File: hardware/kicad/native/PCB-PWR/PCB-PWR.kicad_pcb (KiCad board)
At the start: 4 copper layers, 90 x 60 mm, 66 parts, among them J1 43045-0213, J2 43045-1202, Q1 CSD18540Q5B, U1 LM74700QDBVRQ1, U2 INA226AIDGSR, U3 LMR604403SRAKR, U4 LMR604403SRAKR, U5 TPS7A2018PDBVR

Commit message: pcb-pwr: apply accepted C13-to-C11 routing 009
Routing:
- net VBAT_SYS: track 38.9 -> 70.3 mm
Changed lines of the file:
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@@
+		(net 31)
+	)
+	(segment
+		(start 44 31.8)
+		(end 44 27)
+		(width 3)
+		(layer "F.Cu")
+		(net 31)
+	)
+	(segment
+		(start 44 27)
+		(end 39 27)
+		(width 3)
+		(layer "F.Cu")
+		(net 31)
+	)
+	(segment
+		(start 39 27)
+		(end 39 14)
+		(width 3)
+		(layer "F.Cu")
+		(net 31)
+	)
+	(segment
+		(start 39 14)
+		(end 47.525 14)
+		(width 3)
+		(layer "F.Cu")
 		(net 31)
 	)

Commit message: pcb-pwr: apply accepted 3V8 output bulk routing 010
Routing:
- net 3V8_MODEM: track 0.00 -> 29.0 mm
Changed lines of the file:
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@@
 		(net 31)
+	)
+	(segment
+		(start 64.76 12)
+		(end 67.525 10)
+		(width 3)
+		(layer "F.Cu")
+		(net 3)
+	)
+	(segment
+		(start 64.76 17)
+		(end 67.525 17)
+		(width 3)
+		(layer "F.Cu")
+		(net 3)
+	)
+	(segment
+		(start 67.525 10)
+		(end 67.525 6.8)
+		(width 3)
+		(layer "F.Cu")
+		(net 3)
+	)
+	(segment
+		(start 67.525 6.8)
+		(end 72.525 6.8)
+		(width 3)
+		(layer "F.Cu")
+		(net 3)
+	)
+	(segment
+		(start 72.525 6.8)
+		(end 72.525 7.4)
+		(width 3)
+		(layer "F.Cu")
+		(net 3)
+	)
+	(segment
+		(start 72.525 7.4)
+		(end 72.525 10)
+		(width 0.5)
+		(layer "F.Cu")
+		(net 3)
+	)
+	(segment
+		(start 67.525 17)
+		(end 67.525 20.2)
+		(width 3)
+		(layer "F.Cu")
+		(net 3)
+	)
+	(segment
+		(start 67.525 20.2)
+		(end 72.525 20.2)
+		(width 3)
+		(layer "F.Cu")
+		(net 3)
+	)
+	(segment
+		(start 72.525 20.2)
+		(end 72.525 19.6)
+		(width 3)
+		(layer "F.Cu")
+		(net 3)
+	)
+	(segment
+		(start 72.525 19.6)
+		(end 72.525 17)
+		(width 0.5)
+		(layer "F.Cu")
+		(net 3)
 	)
 	(embedded_fonts no)

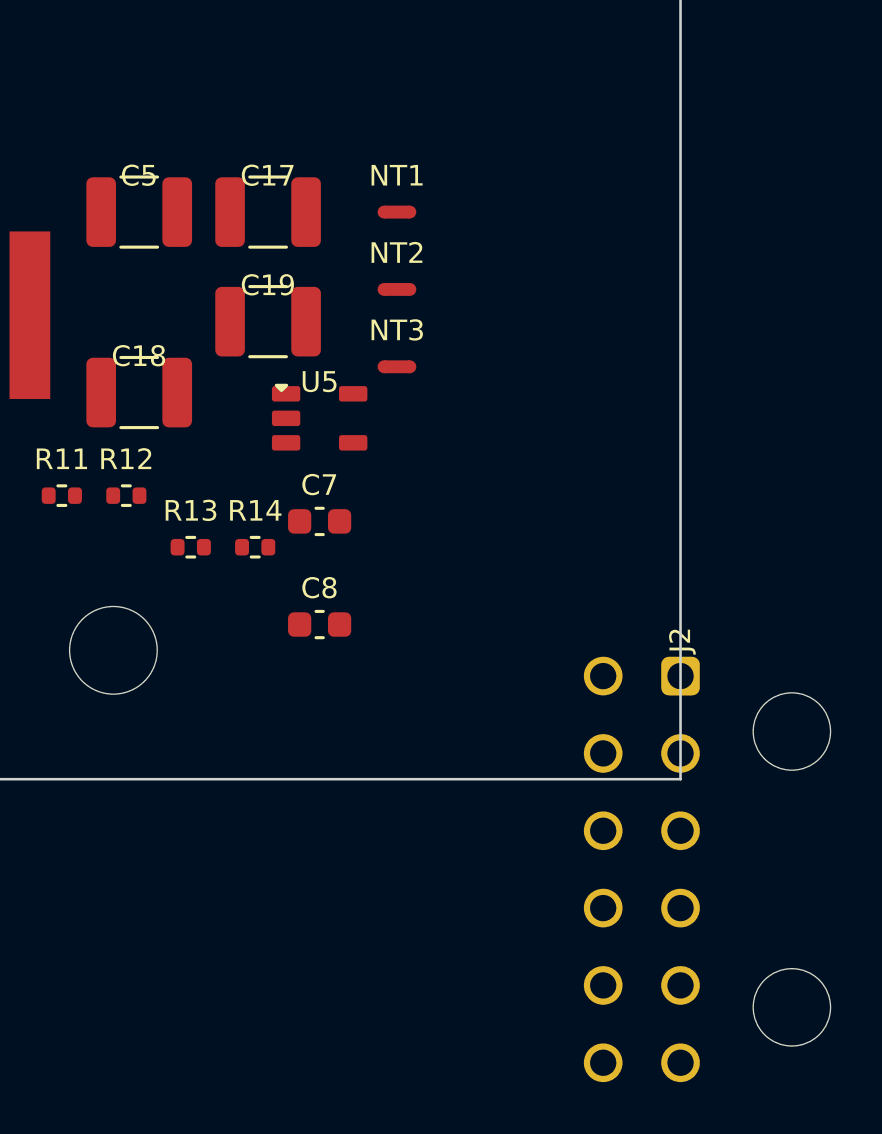
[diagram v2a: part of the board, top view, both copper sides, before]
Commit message: apply: tools/apply_pcb_pwr_j2_placement_eco_003_rev_a.py
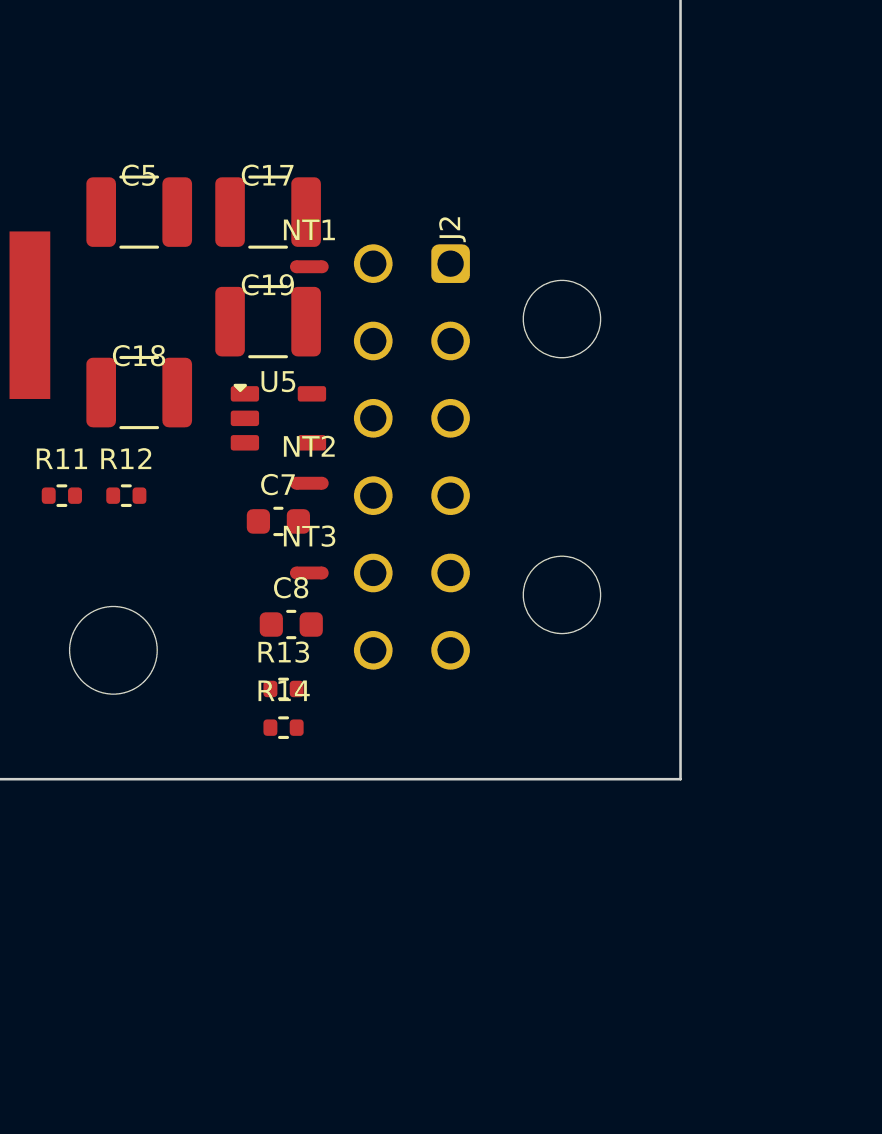
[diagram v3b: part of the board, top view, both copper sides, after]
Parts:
- moved J2 18.3 mm to (81.1, 40.0)
- moved NT3 8.69 mm to (75.6, 52.0)
- moved NT2 8.25 mm to (75.6, 48.5)
- moved R14 7.09 mm to (74.6, 58.0)
- moved R13 6.57 mm to (74.6, 56.5)
- moved NT1 4.01 mm to (75.6, 40.1)
- moved C7 1.60 mm to (74.4, 50.0)
- moved U5 1.60 mm to (74.4, 46.0)
- moved C8 1.10 mm to (74.9, 54.0)
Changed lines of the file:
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@@
 	(footprint "Capacitor_SMD:C_0603_1608Metric"
 		(layer "F.Cu")
-		(at 76 50)
+		(at 74.4 50)
 		(descr "DIONEA_PCB_PWR_REV_A|population=FITTED|zone=AUX_1V8|placement=PROVISIONAL_NOISE_REVIEW_PENDING|authority=PCB_PWR_PASSIVE_AUTHORITY_REV_A.csv")
 		(tags "DIONEA PCB-PWR EVT DIM-003 ACCEPTED NOT FOR MANUFACTURE")
@@
 	(footprint "NetTie:NetTie-2_SMD_Pad0.5mm"
 		(layer "F.Cu")
-		(at 79 38)
+		(at 75.6 40.12)
 		(descr "DIONEA_PCB_PWR_REV_A|population=PCB_FEATURE|zone=GROUND_JOIN|placement=PROVISIONAL_RETURN_REVIEW_PENDING|authority=PCB_PWR_PASSIVE_AUTHORITY_REV_A.csv")
 		(tags "DIONEA PCB-PWR EVT DIM-003 ACCEPTED NOT FOR MANUFACTURE")
@@
 	(footprint "NetTie:NetTie-2_SMD_Pad0.5mm"
 		(layer "F.Cu")
-		(at 79 41)
+		(at 75.6 48.52)
 		(descr "DIONEA_PCB_PWR_REV_A|population=PCB_FEATURE|zone=GROUND_JOIN|placement=PROVISIONAL_RETURN_REVIEW_PENDING|authority=PCB_PWR_PASSIVE_AUTHORITY_REV_A.csv")
 		(tags "DIONEA PCB-PWR EVT DIM-003 ACCEPTED NOT FOR MANUFACTURE")
@@
 	(footprint "Resistor_SMD:R_0402_1005Metric"
 		(layer "F.Cu")
-		(at 71 51)
+		(at 74.6 56.5)
 		(descr "DIONEA_PCB_PWR_REV_A|population=DNP|zone=CONTROL_INTERFACE|placement=PROVISIONAL_I2C_REVIEW_PENDING|authority=PCB_PWR_PASSIVE_AUTHORITY_REV_A.csv")
 		(tags "DIONEA PCB-PWR EVT DIM-003 ACCEPTED NOT FOR MANUFACTURE")
@@
 	(footprint "Resistor_SMD:R_0402_1005Metric"
 		(layer "F.Cu")
-		(at 73.5 51)
+		(at 74.6 58)
 		(descr "DIONEA_PCB_PWR_REV_A|population=DNP|zone=CONTROL_INTERFACE|placement=PROVISIONAL_I2C_REVIEW_PENDING|authority=PCB_PWR_PASSIVE_AUTHORITY_REV_A.csv")
 		(tags "DIONEA PCB-PWR EVT DIM-003 ACCEPTED NOT FOR MANUFACTURE")
@@
 	(footprint "DioneyaMain:Molex_43045-1202_MicroFit-12_RA"
 		(layer "F.Cu")
-		(at 90 56 -90)
+		(at 81.08 40 -90)
 		(descr "DIONEA_PCB_PWR_REV_A|population=FITTED|zone=CONTROL_INTERFACE|placement=PROVISIONAL_SERVICE_CLEARANCE_PENDING|authority=PCB_PWR_FOOTPRINT_AUTHORITY_REV_A.md")
 		(tags "DIONEA PCB-PWR EVT DIM-003 ACCEPTED NOT FOR MANUFACTURE")
@@
 	(footprint "NetTie:NetTie-2_SMD_Pad0.5mm"
 		(layer "F.Cu")
-		(at 79 44)
+		(at 75.6 52)
 		(descr "DIONEA_PCB_PWR_REV_A|population=PCB_FEATURE|zone=GROUND_JOIN|placement=PROVISIONAL_RETURN_REVIEW_PENDING|authority=PCB_PWR_PASSIVE_AUTHORITY_REV_A.csv")
 		(tags "DIONEA PCB-PWR EVT DIM-003 ACCEPTED NOT FOR MANUFACTURE")
@@
 	(footprint "Capacitor_SMD:C_0603_1608Metric"
 		(layer "F.Cu")
-		(at 76 54)
+		(at 74.9 54)
 		(descr "DIONEA_PCB_PWR_REV_A|population=FITTED|zone=AUX_1V8|placement=PROVISIONAL_NOISE_REVIEW_PENDING|authority=PCB_PWR_PASSIVE_AUTHORITY_REV_A.csv")
 		(tags "DIONEA PCB-PWR EVT DIM-003 ACCEPTED NOT FOR MANUFACTURE")
@@
 	(footprint "DioneyaMain:TI_DBV0005A_SOT23-5"
 		(layer "F.Cu")
-		(at 76 46)
+		(at 74.4 46)
 		(descr "DIONEA_PCB_PWR_REV_A|population=FITTED|zone=AUX_1V8|placement=PROVISIONAL_NOISE_REVIEW_PENDING|authority=PCB_PWR_PIN_AUTHORITY_REV_A.csv")
 		(tags "DIONEA PCB-PWR EVT DIM-003 ACCEPTED NOT FOR MANUFACTURE")

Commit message: apply: tools/apply_pcb_pwr_autoroute_011_audit_chain_rev_a.py tools/apply_pcb_pwr_autoroute_011_rev_a.py
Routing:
- net 3V3_DIGITAL: track 0.00 -> 130.3 mm, vias 0 -> 7
- net 3V8_MODEM: track 29.0 -> 143.1 mm, vias 0 -> 1
- net I2C2_SDA: track 0.00 -> 81.1 mm, vias 0 -> 3
- net FAULT: track 0.00 -> 78.3 mm, vias 0 -> 4
- net EN_MODEM: track 0.00 -> 75.9 mm, vias 0 -> 2
- net 1V8_MIC: track 0.00 -> 75.5 mm, vias 0 -> 5
- net I2C2_SCL: track 0.00 -> 74.4 mm, vias 0 -> 3
- net VBAT_PROTECTED: track 0.00 -> 70.8 mm, vias 0 -> 15
- net PG_3V8: track 0.00 -> 66.5 mm, vias 0 -> 3
- net PWR_GOOD: track 0.00 -> 64.7 mm, vias 0 -> 2
- net GND_PWR: track 4.06 -> 66.4 mm, vias 8 -> 191
- net SHUNT_SOURCE_SENSE: track 0.00 -> 47.3 mm, vias 0 -> 4
- net SHUNT_LOAD_SENSE: track 0.00 -> 46.5 mm, vias 0 -> 3
- net VBAT_FUSED: track 0.00 -> 45.9 mm, vias 0 -> 2
- net RT_3V8: track 0.00 -> 23.8 mm, vias 0 -> 4
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- added copper zone on B.Cu, net 3V3_DIGITAL
- added copper zone on F.Cu, net 3V3_DIGITAL
- added copper zone on B.Cu, net 3V8_MODEM
- added copper zone on F.Cu, net 3V8_MODEM
- added copper zone on F.Cu, net GND_DIGITAL
- added copper zone on B.Cu, net GND_MODEM
- added copper zone on F.Cu, net GND_MODEM
- added copper zone on B.Cu, net GND_PWR
- added copper zone on F.Cu, net GND_PWR
- added copper zone on In2.Cu, net GND_PWR
- added copper zone on B.Cu, net VBAT_FUSED
- added copper zone on F.Cu, net VBAT_FUSED
- added copper zone on B.Cu, net VBAT_PROTECTED
- added copper zone on F.Cu, net VBAT_PROTECTED
- added copper zone on F.Cu, net VBAT_RAW
- added copper zone on B.Cu, net VBAT_SYS
- added copper zone on F.Cu, net VBAT_SYS

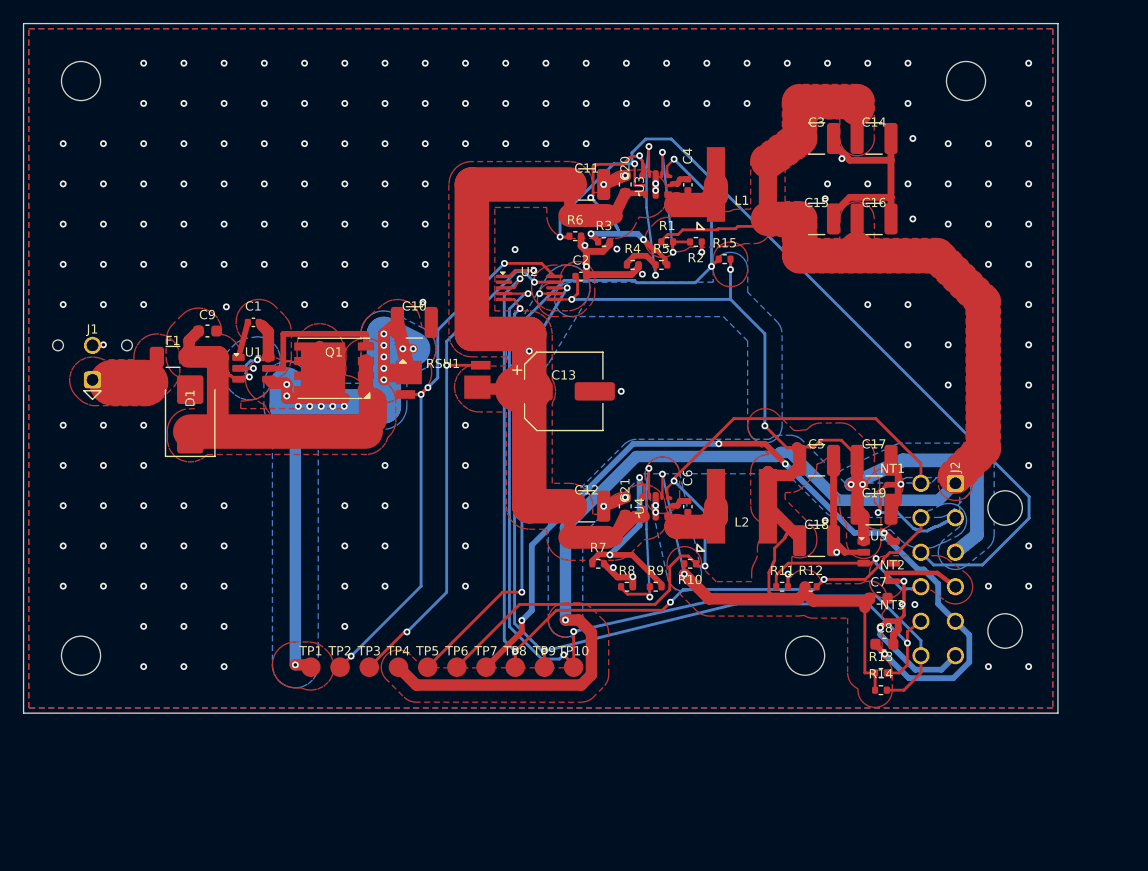
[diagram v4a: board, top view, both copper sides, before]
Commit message: apply: tools/apply_pcb_pwr_eco_005_audit_chain_rev_a.py tools/apply_pcb_pwr_eco_005_rev_a.py
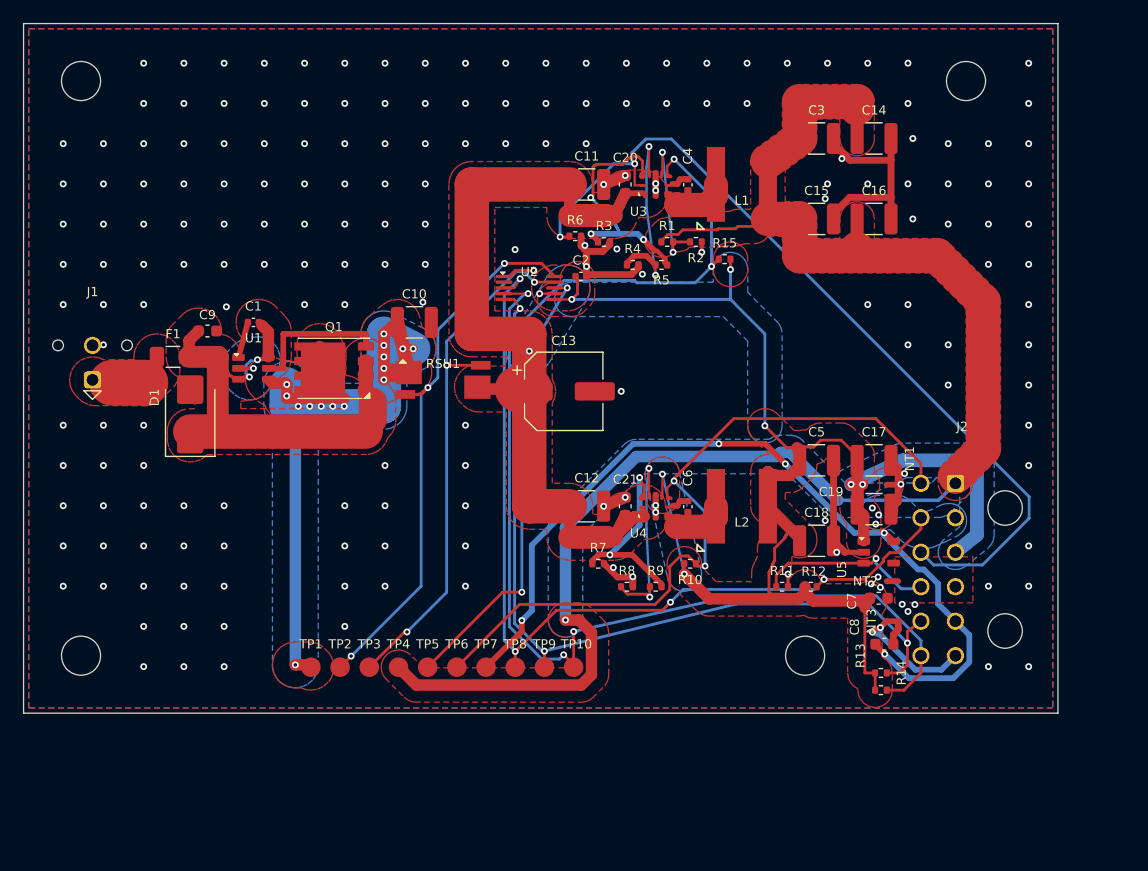
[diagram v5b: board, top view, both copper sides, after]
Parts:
- turned NT2 to 180 degrees
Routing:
- net GND_MODEM: track 9.93 -> 0.00 mm, vias 1 -> 3
- net GND_DIGITAL: track 7.10 -> 0.00 mm
- net GND_PWR: track 66.4 -> 62.2 mm, vias 191 -> 195
- net RT_3V8: track 23.8 -> 22.1 mm, vias 4 -> 3
- net GND_MIC: track 9.71 -> 11.2 mm, vias 1 -> 2
- net SHUNT_SOURCE_SENSE: track 47.3 -> 48.1 mm, vias 4 -> 3
